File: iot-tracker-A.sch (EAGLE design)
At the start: 22 parts, among them U1 ESP-WROOM-02, U2 TPL5111DDCR, U3 MCP1640T-I_CHY

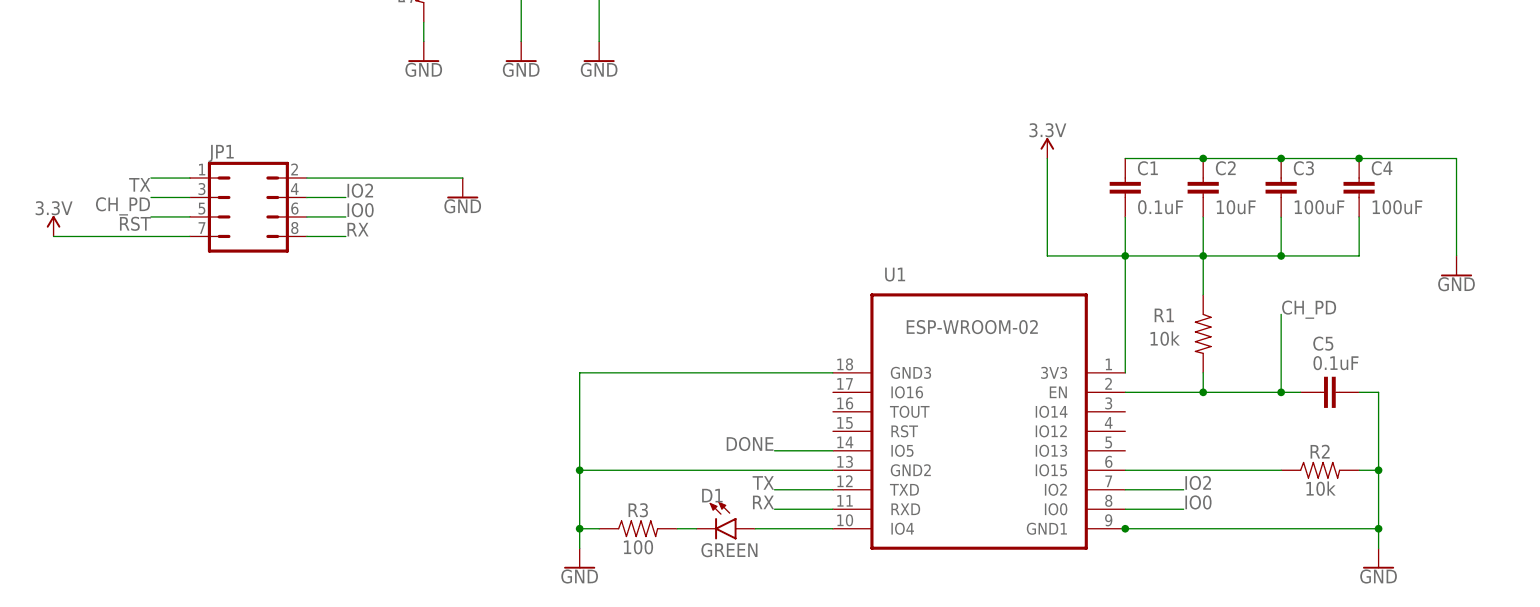
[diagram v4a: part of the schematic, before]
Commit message: Changed pin header from 2x4 to 1x6
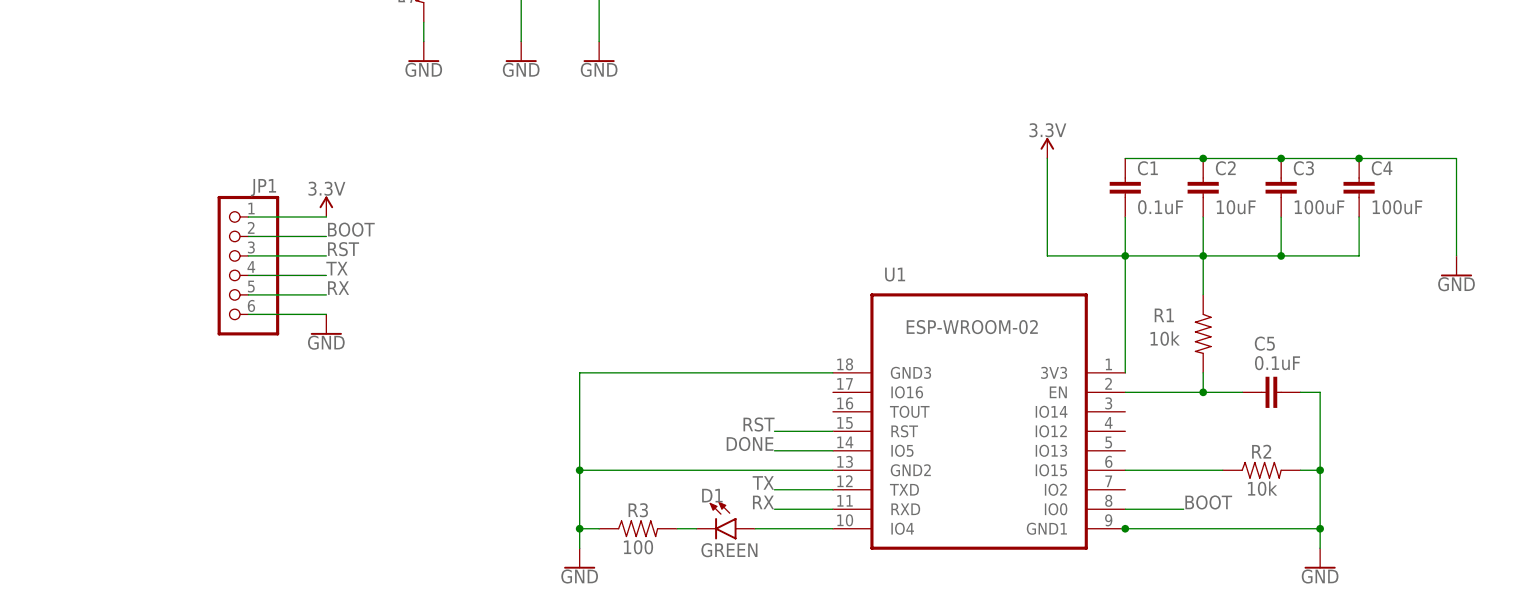
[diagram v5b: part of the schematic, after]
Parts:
- JP1: device jumper:JP4Q -> pinhead:PINHD-1X6
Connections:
- removed net CH_PD: C5.2, JP1.3, R1.2, U1.EN
- removed net IO0: JP1.6, U1.IO0
- removed net IO2: JP1.4, U1.IO2
- new net BOOT: JP1.2, U1.IO0
- new net EN: C5.2, R1.2, U1.EN
- net 3.3V: now also JP1.1; no longer JP1.7
- net GND: now also JP1.6; no longer JP1.2
- net RST: now also JP1.3, U1.RST; no longer JP1.5
- net RX: now also JP1.5; no longer JP1.8
- net TX: now also JP1.4; no longer JP1.1
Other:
- moved on the sheet: C5, R2

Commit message: Added battery pin headers
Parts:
- added JP2: (no value), pinhead:PINHD-1X2
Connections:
- net GND: now also JP2.2
- net V_BATT: now also JP2.1
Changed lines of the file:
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@@
 <part name="SUPPLY6" library="SparkFun-PowerSymbols" library_urn="urn:adsk.eagle:library:530" deviceset="3.3V" device=""/>
 <part name="GND1" library="SparkFun-PowerSymbols" library_urn="urn:adsk.eagle:library:530" deviceset="GND" device=""/>
+<part name="JP2" library="pinhead" library_urn="urn:adsk.eagle:library:325" deviceset="PINHD-1X2" device="" package3d_urn="urn:adsk.eagle:package:22435/2"/>
+<part name="SUPPLY7" library="SparkFun-PowerSymbols" library_urn="urn:adsk.eagle:library:530" deviceset="V_BATT" device=""/>
+<part name="GND10" library="SparkFun-PowerSymbols" library_urn="urn:adsk.eagle:library:530" deviceset="GND" device=""/>
 </parts>
 <sheets>
@@
 <instance part="GND1" gate="1" x="-101.6" y="0" smashed="yes" rot="MR0">
 <attribute name="VALUE" x="-101.6" y="-0.254" size="1.778" layer="96" rot="MR0" align="top-center"/>
+</instance>
+<instance part="JP2" gate="G$1" x="-114.3" y="-15.24" smashed="yes" rot="MR0">
+<attribute name="NAME" x="-107.95" y="-9.525" size="1.778" layer="95" rot="MR0"/>
+<attribute name="VALUE" x="-107.95" y="-20.32" size="1.778" layer="96" rot="MR0"/>
+</instance>
+<instance part="SUPPLY7" gate="G$1" x="-101.6" y="-12.7" smashed="yes">
+<attribute name="VALUE" x="-101.6" y="-9.906" size="1.778" layer="96" align="bottom-center"/>
+</instance>
+<instance part="GND10" gate="1" x="-101.6" y="-17.78" smashed="yes" rot="MR0">
+<attribute name="VALUE" x="-101.6" y="-18.034" size="1.778" layer="96" rot="MR0" align="top-center"/>
 </instance>
 </instances>
@@
 <wire x1="-111.76" y1="2.54" x2="-101.6" y2="2.54" width="0.1524" layer="91"/>
 <pinref part="GND1" gate="1" pin="GND"/>
+</segment>
+<segment>
+<pinref part="JP2" gate="G$1" pin="2"/>
+<wire x1="-111.76" y1="-15.24" x2="-101.6" y2="-15.24" width="0.1524" layer="91"/>
+<pinref part="GND10" gate="1" pin="GND"/>
 </segment>
 </net>
@@
 <pinref part="SUPPLY3" gate="G$1" pin="V_BATT"/>
 </segment>
-</net>
+<segment>
+<pinref part="JP2" gate="G$1" pin="1"/>
+<wire x1="-111.76" y1="-12.7" x2="-101.6" y2="-12.7" width="0.1524" layer="91"/>
+<pinref part="SUPPLY7" gate="G$1" pin="V_BATT"/>
+</segment>
+</net>

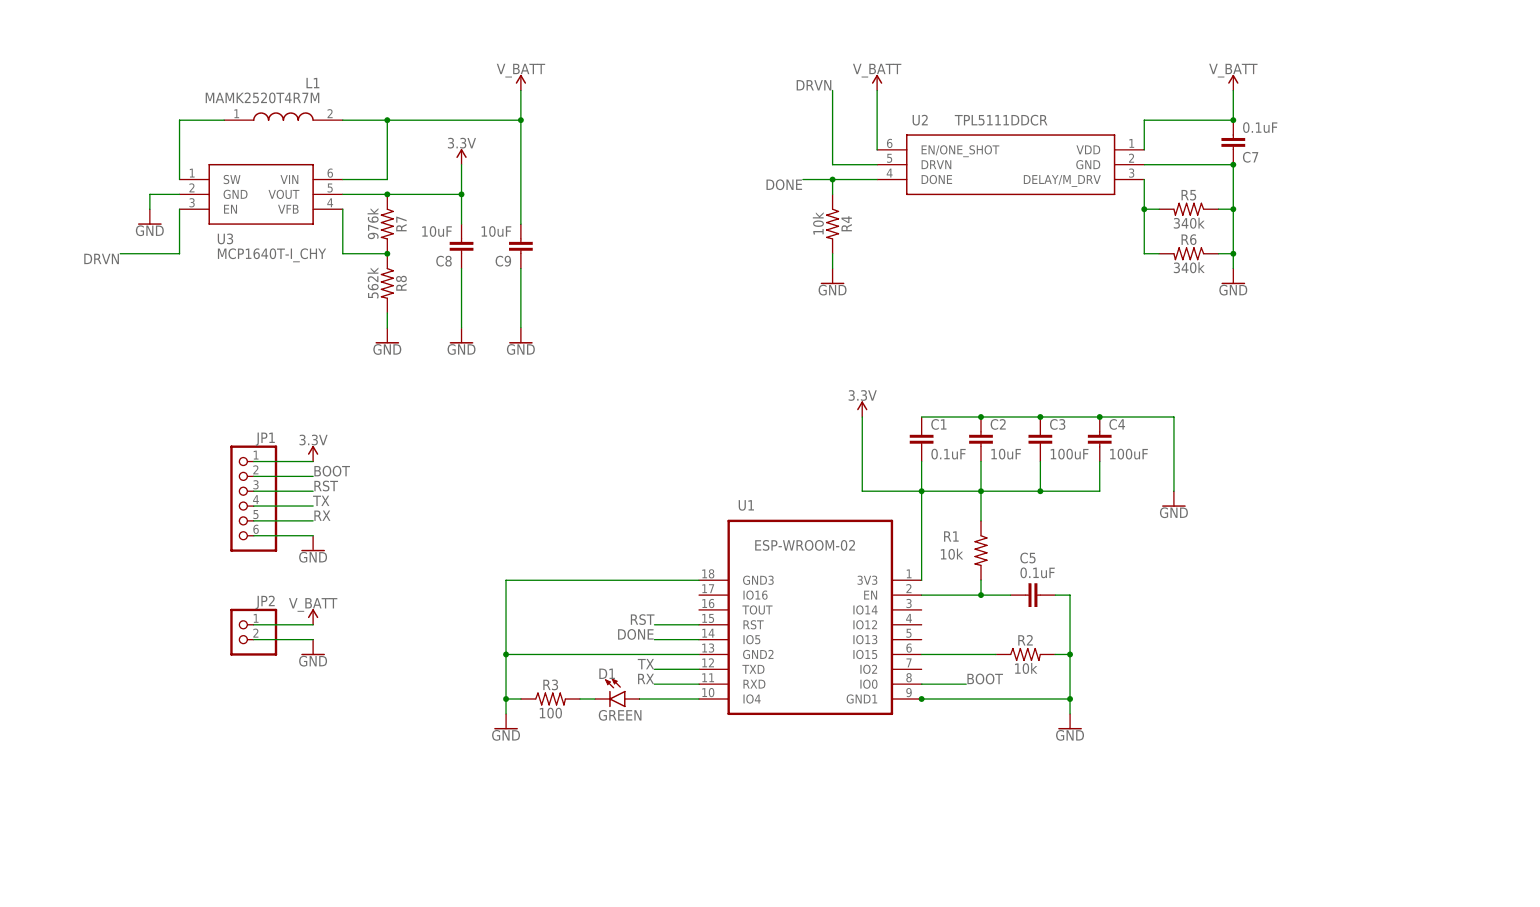
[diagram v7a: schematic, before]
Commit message: Reorganized component placement and consolidated headers into a single 1x8 part
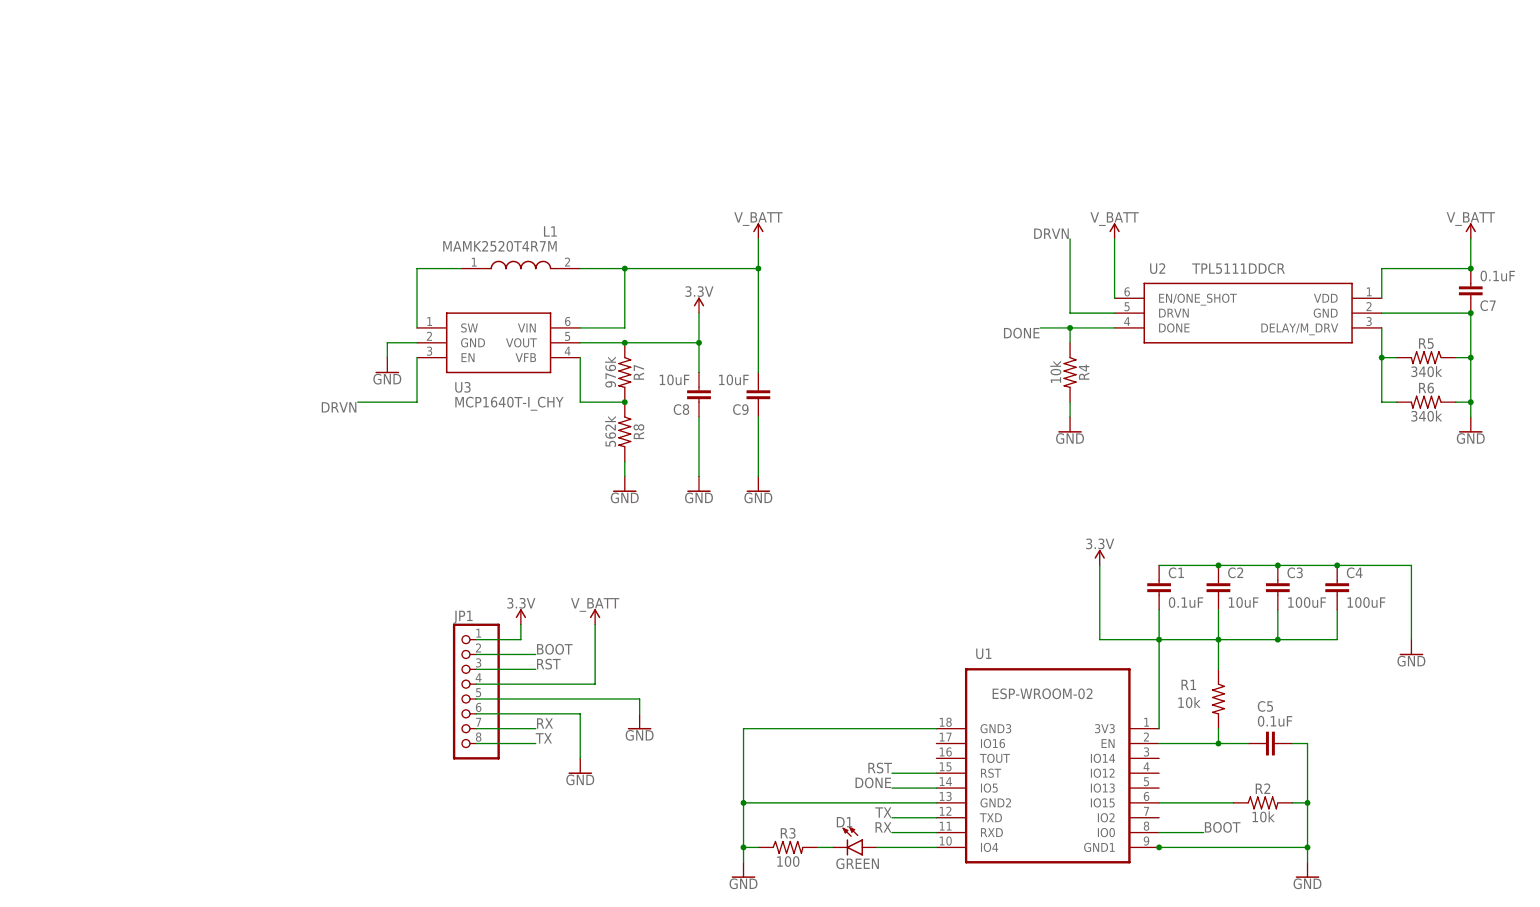
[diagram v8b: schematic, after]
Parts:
- removed JP2: (no value), pinhead:PINHD-1X2
- JP1: device pinhead:PINHD-1X6 -> pinhead:PINHD-1X8
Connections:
- net GND: now also JP1.5; no longer JP2.2
- net RX: now also JP1.7; no longer JP1.5
- net TX: now also JP1.8; no longer JP1.4
- net V_BATT: now also JP1.4; no longer JP2.1
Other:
- moved on the sheet: C1, C2, C3, C4, C5, C7, C8, C9, D1, L1, R1, R2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
